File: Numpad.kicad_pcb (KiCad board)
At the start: 2 copper layers, 94 x 162.6 mm, 68 parts, among them J1 SWD, J2 USB4085-GF-A_REVA, SW1 SW_Push, SW10 SW_Push, SW11 SW_Push, SW12 SW_Push, SW13 SW_Push, SW14 SW_Push, SW15 SW_Push, SW16 SW_Push, SW17 SW_Push, SW18 SW_Push, SW19 SW_Push, SW2 SW_Push, SW20 SW_Push, SW21 SW_Push, SW3 SW_Push, SW4 SW_Push, SW5 SW_Push, SW6 SW_Push, SW7 SW_Push, SW8 SW_Push, SW9 SW_Push, U1 SRV05-4, U2 STM32F103C8Tx, U3 XC6206PxxxMR, Y1 8MHz

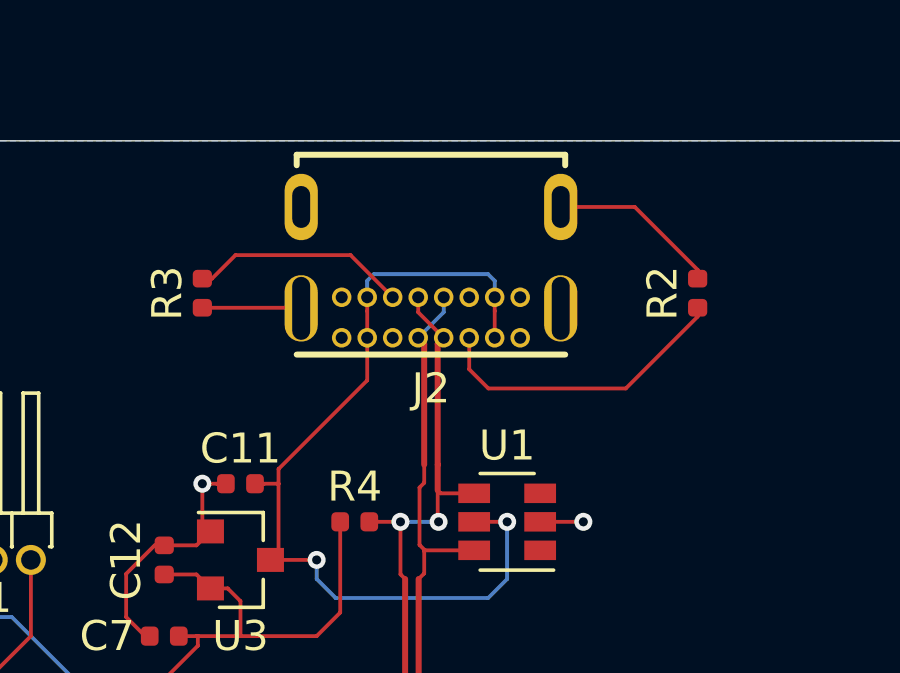
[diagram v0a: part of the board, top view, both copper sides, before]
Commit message: 0.3: removed dependencies on external libraries
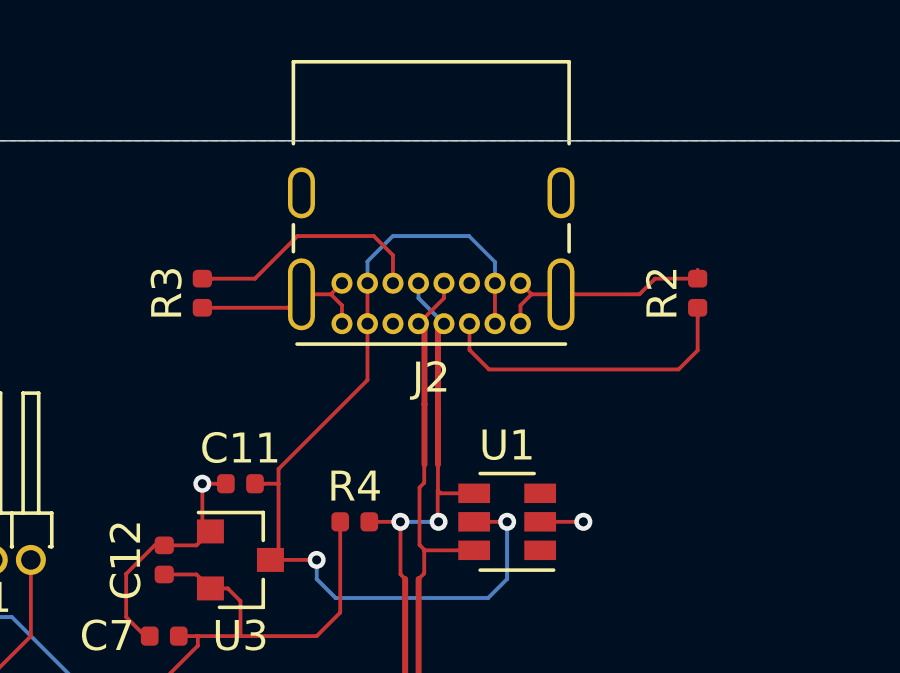
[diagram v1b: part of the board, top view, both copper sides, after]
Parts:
- J2: value USB4085-GF-A_REVA -> USB_C_Receptacle_USB2.0; footprint USB4085:GCT_USB4085-GF-A_REVA -> Connector_USB:USB_C_Receptacle_GCT_USB4085
- moved J2 4.64 mm to (66.5, 22.6)
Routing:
- net GND: track 49.4 -> 54.2 mm
- net +5V: track 30.0 -> 31.3 mm
- net /CC2: track 7.25 -> 8.46 mm
- net /CC1: track 10.2 -> 10.7 mm

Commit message: v0.4
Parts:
- removed D1, D10, D11, D12, D13, D14, D15, D16, D17, D18, D19, D2, D20, D21, D3, D4, D5, D6, D7, D8, D9: 1N4148, Diode_SMD:D_SOD-123
- removed SW1, SW10, SW11, SW12, SW13, SW14, SW15, SW16, SW17, SW18, SW19, SW2, SW3, SW4, SW5, SW7, SW8, SW9: SW_Push, Button_Switch_Keyboard:SW_Cherry_MX_1.00u_PCB
- removed SW20, SW21: SW_Push, Button_Switch_Keyboard:SW_Cherry_MX_2.00u_Vertical_PCB
- removed SW6: SW_Push, Button_Switch_Keyboard:SW_Cherry_MX_2.00u_PCB
- added D_0: 1N4148, Diode_SMD:D_SOD-123, B.Cu at (126.4, 141.6)
- added D_1: 1N4148, Diode_SMD:D_SOD-123, B.Cu at (116.8, 122.6)
- added D_2: 1N4148, Diode_SMD:D_SOD-123, B.Cu at (135.9, 122.6)
- added D_3: 1N4148, Diode_SMD:D_SOD-123, B.Cu at (154.9, 122.6)
- added D_4: 1N4148, Diode_SMD:D_SOD-123, B.Cu at (116.8, 103.5)
- added D_5: 1N4148, Diode_SMD:D_SOD-123, B.Cu at (135.9, 103.5)
- added D_6: 1N4148, Diode_SMD:D_SOD-123, B.Cu at (154.9, 103.5)
- added D_7: 1N4148, Diode_SMD:D_SOD-123, B.Cu at (116.8, 84.5)
- added D_8: 1N4148, Diode_SMD:D_SOD-123, B.Cu at (135.9, 84.5)
- added D_9: 1N4148, Diode_SMD:D_SOD-123, B.Cu at (154.9, 84.5)
- added D_BKSP1: 1N4148, Diode_SMD:D_SOD-123, B.Cu at (168.3, 38.1)
- added D_DOT1: 1N4148, Diode_SMD:D_SOD-123, B.Cu at (154.9, 141.6)
- added D_ENTER1: 1N4148, Diode_SMD:D_SOD-123, B.Cu at (161.9, 132.7)
- added D_ESC1: 1N4148, Diode_SMD:D_SOD-123, B.Cu at (116.8, 40.0)
- added D_FN1: 1N4148, Diode_SMD:D_SOD-123, B.Cu at (154.9, 40.0)
- added D_MINUS1: 1N4148, Diode_SMD:D_SOD-123, B.Cu at (174.0, 65.4)
- added D_NUMLK1: 1N4148, Diode_SMD:D_SOD-123, B.Cu at (116.8, 65.4)
- added D_PLUS1: 1N4148, Diode_SMD:D_SOD-123, B.Cu at (161.9, 94.6)
- added D_SLASH1: 1N4148, Diode_SMD:D_SOD-123, B.Cu at (139.7, 70.0)
- added D_STAR1: 1N4148, Diode_SMD:D_SOD-123, B.Cu at (158.5, 68.0)
- added D_TAB1: 1N4148, Diode_SMD:D_SOD-123, B.Cu at (128.3, 38.7)
- added SW_0: SW_Push, Keebio-Parts:MX-Alps-Choc-2U, F.Cu at (120.7, 149.2)
- added SW_1: SW_Push, Keebio-Parts:MX-Alps-Choc-1U, F.Cu at (111.1, 130.2)
- added SW_2: SW_Push, Keebio-Parts:MX-Alps-Choc-1U, F.Cu at (130.2, 130.2)
- added SW_3: SW_Push, Keebio-Parts:MX-Alps-Choc-1U, F.Cu at (149.2, 130.2)
- added SW_4: SW_Push, Keebio-Parts:MX-Alps-Choc-1U, F.Cu at (111.1, 111.1)
- added SW_5: SW_Push, Keebio-Parts:MX-Alps-Choc-1U, F.Cu at (130.2, 111.1)
- added SW_6: SW_Push, Keebio-Parts:MX-Alps-Choc-1U, F.Cu at (149.2, 111.1)
- added SW_7: SW_Push, Keebio-Parts:MX-Alps-Choc-1U, F.Cu at (111.1, 92.1)
- added SW_8: SW_Push, Keebio-Parts:MX-Alps-Choc-1U, F.Cu at (130.2, 92.1)
- added SW_9: SW_Push, Keebio-Parts:MX-Alps-Choc-1U, F.Cu at (149.2, 92.1)
- added SW_BKSP1: SW_Push, Keebio-Parts:MX-Alps-Choc-1U, F.Cu at (168.3, 47.6)
- added SW_DOT1: SW_Push, Keebio-Parts:MX-Alps-Choc-1U, F.Cu at (149.2, 149.2)
- added SW_ENTER1: SW_Push, Keebio-Parts:MX-Alps-Choc-2U, F.Cu at (168.3, 139.7)
- added SW_ESC1: SW_Push, Keebio-Parts:MX-Alps-Choc-1U, F.Cu at (111.1, 47.6)
- added SW_FN1: SW_Push, Keebio-Parts:MX-Alps-Choc-1U, F.Cu at (149.2, 47.6)
- added SW_MINUS1: SW_Push, Keebio-Parts:MX-Alps-Choc-1U, F.Cu at (168.3, 73.0)
- added SW_NUMLK1: SW_Push, Keebio-Parts:MX-Alps-Choc-1U, F.Cu at (111.1, 73.0)
- added SW_PLUS1: SW_Push, Keebio-Parts:MX-Alps-Choc-2U, F.Cu at (168.3, 101.6)
- added SW_SLASH1: SW_Push, Keebio-Parts:MX-Alps-Choc-1U, F.Cu at (130.2, 73.0)
- added SW_STAR1: SW_Push, Keebio-Parts:MX-Alps-Choc-1U, F.Cu at (149.2, 73.0)
- added SW_TAB1: SW_Push, Keebio-Parts:MX-Alps-Choc-1U, F.Cu at (130.2, 47.6)
- C1, C10, C11, C12, C2, C3, C4, C5, C6, C7, C8, C9, J2, R1, R2, R3, R4, U1, U2, U3, Y1: moved to B.Cu
- H1, H2, H3, H4: value MountingHole_Pad -> MountingHole; footprint MountingHole:MountingHole_3.2mm_M3_Pad -> MountingHole:MountingHole_3.2mm_M3
- moved C9 127.2 mm to (156.8, 62.0)
- moved C8 127.1 mm to (156.8, 58.6)
- moved Y1 122.4 mm to (154.5, 60.4)
- moved C10 112.8 mm to (148.5, 60.0), turned to 180 degrees
- moved C5 112.8 mm to (149.0, 61.5), turned to 90 degrees
- moved C6 111.6 mm to (148.0, 61.5), turned to 90 degrees
- moved C1 110.7 mm to (148.0, 56.5)
- moved C4 105.8 mm to (145.5, 54.0)
- moved R1 101.1 mm to (142.5, 54.0), turned to 180 degrees
- moved U2 100.0 mm to (142.2, 59.7), turned to 180 degrees
- moved C7 98.4 mm to (150.0, 57.0), turned to 180 degrees
- moved C2 94.1 mm to (139.0, 65.5)
- moved R3 91.7 mm to (146.1, 38.1), turned to 270 degrees
- moved C3 89.3 mm to (138.0, 55.0), turned to 270 degrees
- moved C12 89.3 mm to (141.0, 53.0), turned to 180 degrees
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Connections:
- H1 pad 1: GND -> (no net)
- H2 pad 1: GND -> (no net)
- H3 pad 1: GND -> (no net)
- H4 pad 1: GND -> (no net)
- J2 pad A8: Net-(J2-PadA8) -> (no net)
- J2 pad B8: Net-(J2-PadB8) -> (no net)
- U1 pad 1: Net-(U1-Pad1) -> (no net)
- U1 pad 3: Net-(U1-Pad3) -> (no net)
- U2 pad 10: Net-(U2-Pad10) -> (no net)
- U2 pad 11: Net-(U2-Pad11) -> (no net)
- U2 pad 12: Net-(U2-Pad12) -> col4
- U2 pad 13: Net-(U2-Pad13) -> col3
- U2 pad 14: Net-(U2-Pad14) -> (no net)
- U2 pad 15: Net-(U2-Pad15) -> (no net)
- U2 pad 16: Net-(U2-Pad16) -> (no net)
- U2 pad 2: Net-(U2-Pad2) -> (no net)
- U2 pad 20: row3 -> (no net)
- U2 pad 22: row1 -> row3
- U2 pad 25: col4 -> col2
- U2 pad 26: col3 -> col1
- U2 pad 27: col2 -> (no net)
- U2 pad 28: col1 -> (no net)
- U2 pad 29: Net-(U2-Pad29) -> (no net)
- U2 pad 3: Net-(U2-Pad3) -> (no net)
- U2 pad 30: Net-(U2-Pad30) -> (no net)
- U2 pad 31: Net-(U2-Pad31) -> (no net)
- U2 pad 38: Net-(U2-Pad38) -> (no net)
- U2 pad 39: Net-(U2-Pad39) -> (no net)
- U2 pad 4: Net-(U2-Pad4) -> (no net)
- U2 pad 40: Net-(U2-Pad40) -> (no net)
- U2 pad 41: Net-(U2-Pad41) -> (no net)
- U2 pad 42: Net-(U2-Pad42) -> (no net)
- U2 pad 43: Net-(U2-Pad43) -> (no net)
- U2 pad 45: Net-(U2-Pad45) -> (no net)
- U2 pad 46: Net-(U2-Pad46) -> row1
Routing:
- net row3: track 140.1 -> 71.8 mm, vias 0 -> 3
- net row5: track 178.8 -> 112.2 mm, vias 0 -> 2
- net row6: track 174.8 -> 113.6 mm, vias 0 -> 2
- net row4: track 136.5 -> 78.6 mm, vias 0 -> 2
- net Net-(J1-Pad2): track 4.79 -> 37.0 mm, vias 0 -> 2
- net col4: track 156.5 -> 128.7 mm, vias 2 -> 1
- net VBAT: track 75.9 -> 51.0 mm, vias 3 -> 5
- net col3: track 145.4 -> 120.6 mm, vias 2 -> 0
- net col1: track 124.7 -> 149.2 mm
- net row2: track 116.8 -> 93.2 mm
- net Net-(J1-Pad3): track 9.18 -> 31.0 mm, vias 0 -> 1
- net GND: track 54.2 -> 35.8 mm, vias 6 -> 15
- net Net-(D_TAB1-Pad2): track 0.00 -> 8.66 mm
- net Net-(D_BKSP1-Pad2): track 0.00 -> 8.37 mm
- net Net-(D21-Pad2): track 8.01 -> 0.00 mm
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- added copper zone on F.Cu, net GND
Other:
- board size 94 x 162.6 mm -> 82.6 x 127 mm
- net class Power added: clearance 0.127, trace_width 0.2, via_dia 0.6, via_drill 0.3
- board text added: "NumpadA v0.4 Standalone by Inexpensive Computers"
- board text added: "https://b.inexcomp.com"
- board text removed: "NumpadA v0.3 Standalone by Inexpensive Computers"

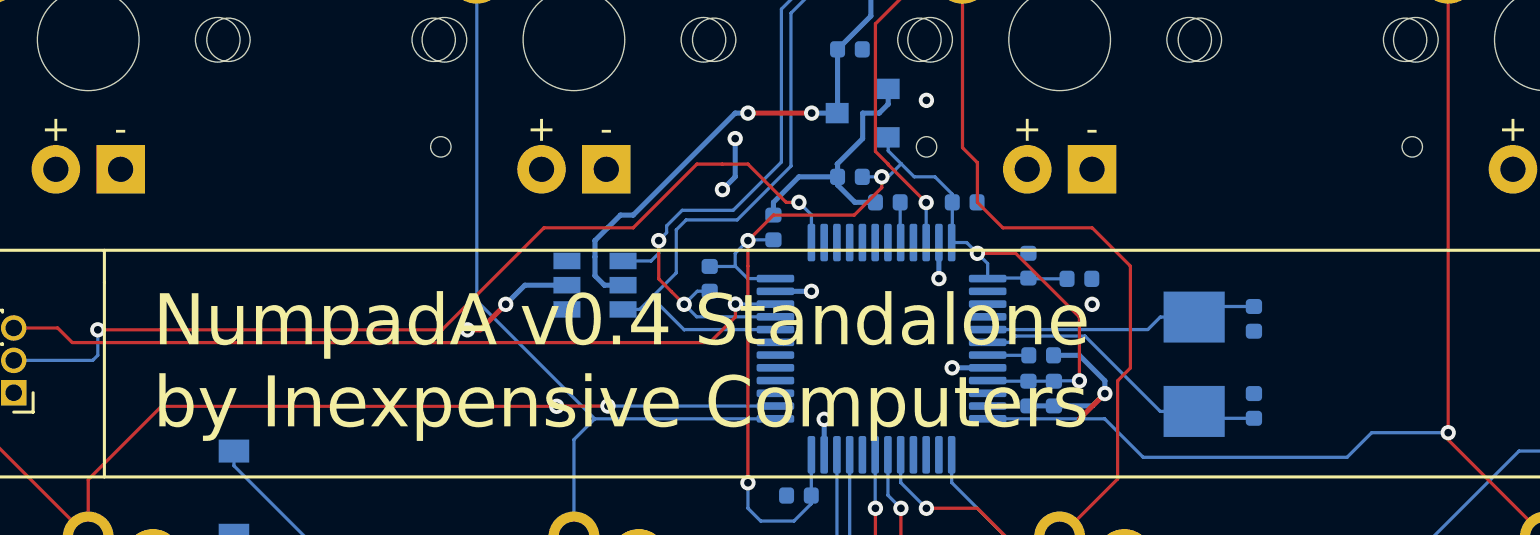
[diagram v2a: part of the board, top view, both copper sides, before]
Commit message: Tuned USB differential pair skew
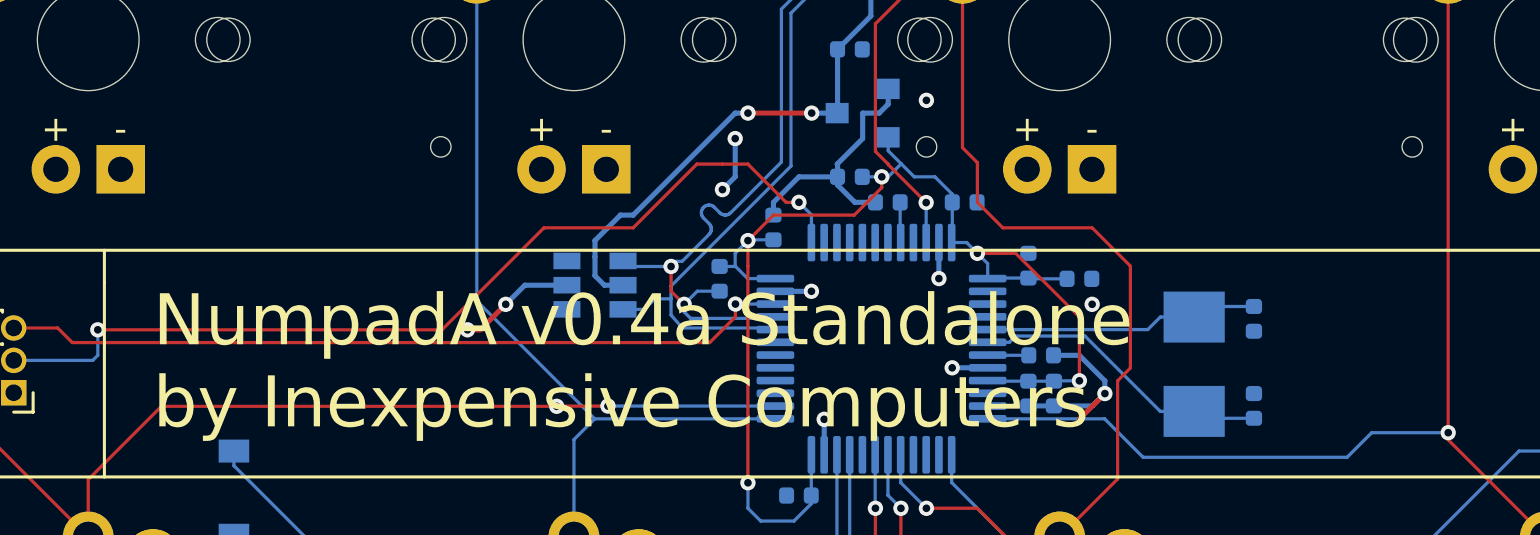
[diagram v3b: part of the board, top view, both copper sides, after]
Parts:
- moved R4 0.39 mm to (135.9, 57.0)
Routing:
- net DA-: track 29.1 -> 28.1 mm
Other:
- board text added: "NumpadA v0.4a Standalone by Inexpensive Computers"
- board text removed: "NumpadA v0.4 Standalone by Inexpensive Computers"

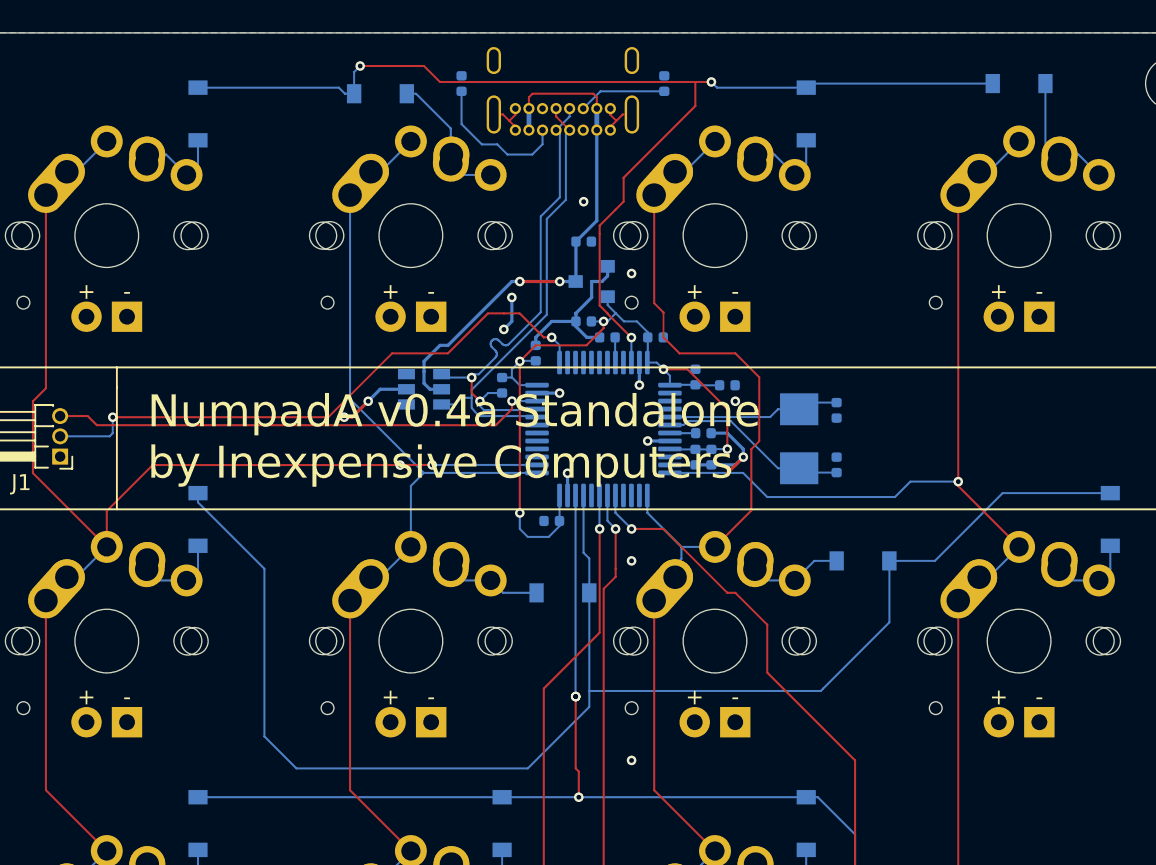
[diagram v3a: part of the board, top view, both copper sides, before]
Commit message: Widened power traces, fixed some routing
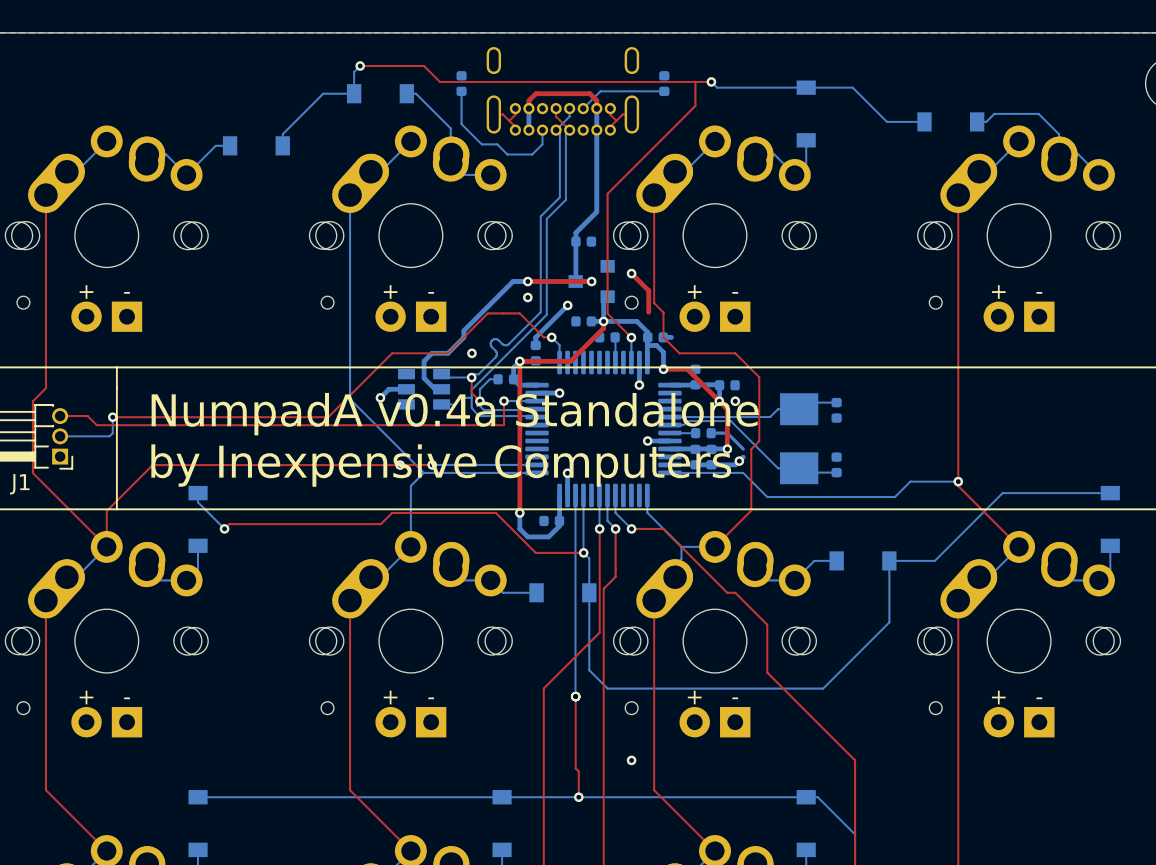
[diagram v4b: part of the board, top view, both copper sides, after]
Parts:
- moved D_BKSP1 4.90 mm to (164.0, 40.5)
- moved D_ESC1 4.17 mm to (120.5, 42.0), turned to 180 degrees
- moved R4 0.44 mm to (136.1, 56.6), turned to 180 degrees
- turned C10 to 0 degrees
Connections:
- net Net-(C8-Pad1) renamed PD0
- net Net-(C9-Pad1) renamed PD1
- net Net-(J1-Pad2) renamed SWDCLK
- net Net-(J1-Pad3) renamed SWDIO
- net Net-(R1-Pad1) renamed BOOT0
- C10 pad 1: GND -> NRST
- C10 pad 2: Net-(C10-Pad2) -> GND
- U2 pad 7: Net-(C10-Pad2) -> NRST
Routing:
- net row2: track 93.2 -> 78.4 mm, vias 0 -> 2
- net GND: track 35.8 -> 25.4 mm, vias 15 -> 13
- net row1: track 73.0 -> 65.8 mm
- net Net-(D_BKSP1-Pad2): track 8.37 -> 11.9 mm
- net +5V: track 32.8 -> 34.6 mm
- net Net-(C10-Pad2): track 1.62 -> 0.00 mm
- net NRST: track 0.00 -> 1.62 mm
- net Net-(D_ESC1-Pad2): track 5.46 -> 6.47 mm
- net SWDIO: track 31.0 -> 31.6 mm
- net DA+: track 30.3 -> 30.8 mm
- net VBAT: track 50.6 -> 51.0 mm, vias 5 -> 6
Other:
- net class Power: trace_width 0.2 -> 0.3

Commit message: Annotated and reformatted schematic
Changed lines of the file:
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@@
   (segment (start 150.75 61.75) (end 151 61.5) (width 0.3) (layer B.Cu) (net 11))
   (via (at 150.75 61.75) (size 0.6) (drill 0.3) (layers F.Cu B.Cu) (net 11))
-  (segment (start 145.985 54) (end 146.5 54) (width 0.3) (layer B.Cu) (net 11))
   (segment (start 144.49 55.5775) (end 144.49 56.99) (width 0.3) (layer B.Cu) (net 11))
   (segment (start 148 61.985) (end 149 61.985) (width 0.3) (layer B.Cu) (net 11))
   (segment (start 145.07449 51.07449) (end 145.07449 52.42551) (width 0.3) (layer F.Cu) (net 11))
   (segment (start 144 50) (end 145.07449 51.07449) (width 0.3) (layer F.Cu) (net 11))
+  (segment (start 145.985 54) (end 146.28 54) (width 0.3) (layer B.Cu) (net 11))
   (segment (start 154.915 58.085) (end 154.5 58.5) (width 0.127) (layer B.Cu) (net 39))
   (segment (start 156.845 58.085) (end 154.915 58.085) (width 0.127) (layer B.Cu) (net 39))
